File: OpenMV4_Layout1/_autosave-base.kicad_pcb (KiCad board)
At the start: 4 copper layers, 35.6 x 44.5 mm, 57 parts, among them M1 9774030243R, M2 9774030243R, Q1 BSS138, Q2 Si2301BDS, U1 STM32H743VIT6, U5 TPS731XX, U8 PAM2305AABADJ, X1 MF-CON-MICROUSB-RIGHT, X2 USD-1040310811, X3 DF12-36-DS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

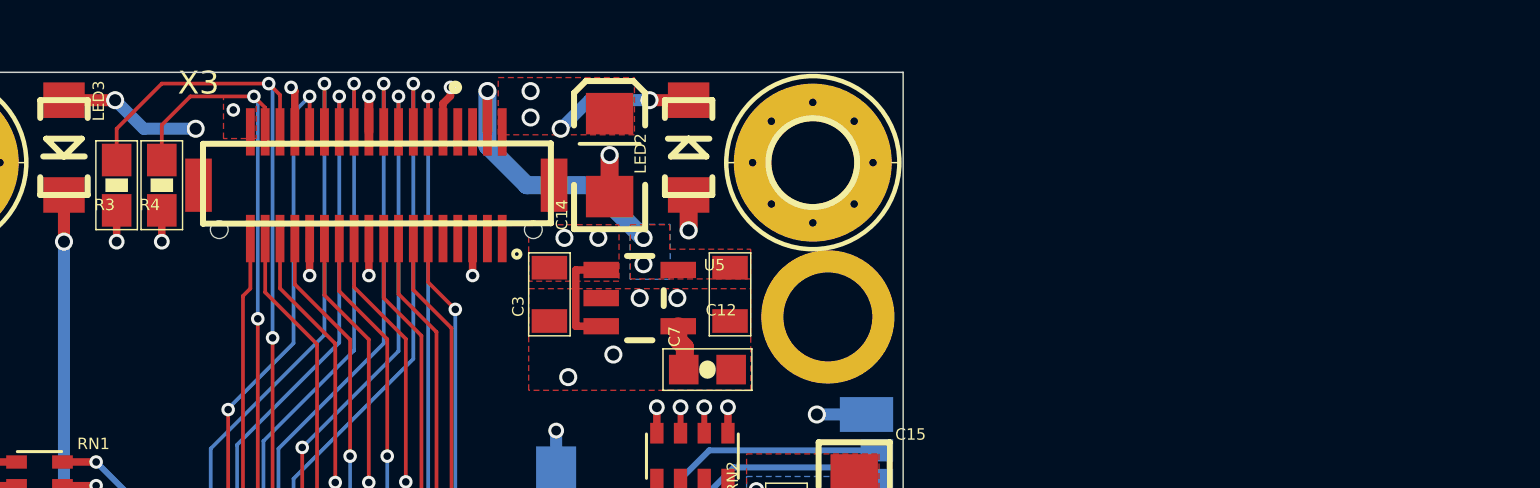
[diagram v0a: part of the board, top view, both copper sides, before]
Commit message: Swapped image sensor connector to opposite side
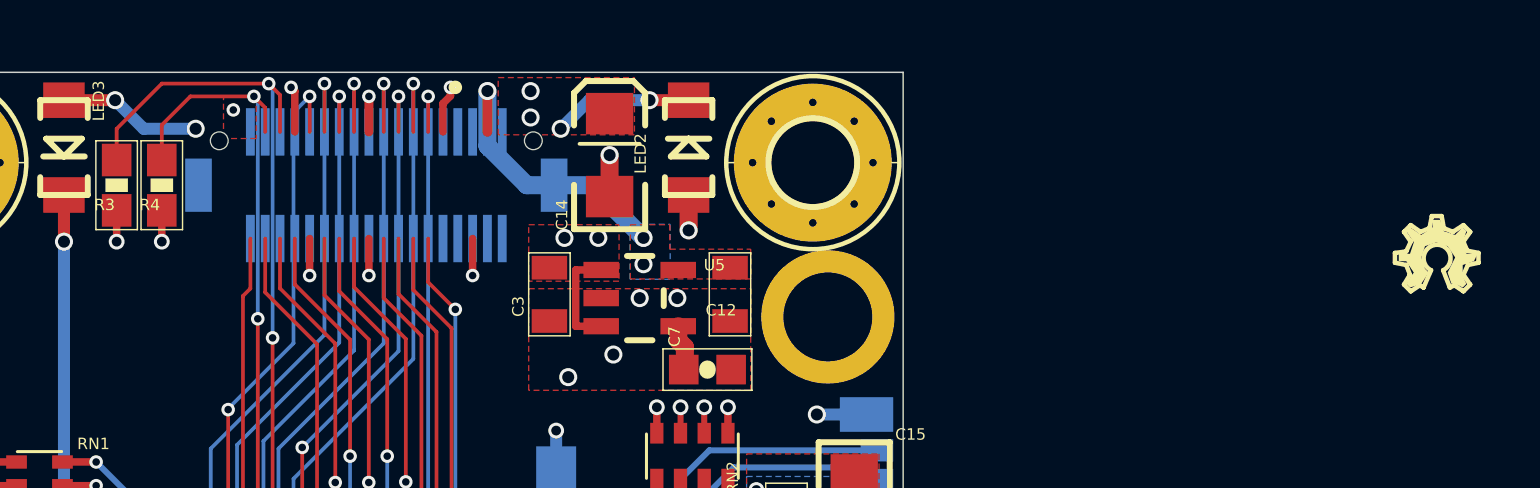
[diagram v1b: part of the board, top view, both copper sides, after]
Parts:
- added LOGO1: OSHW_LOGO_FILLX0100-NT, base:OSHW_FILLX100_NOTEXT, F.Cu at (182.9, 90.2)
- X3: moved to B.Cu

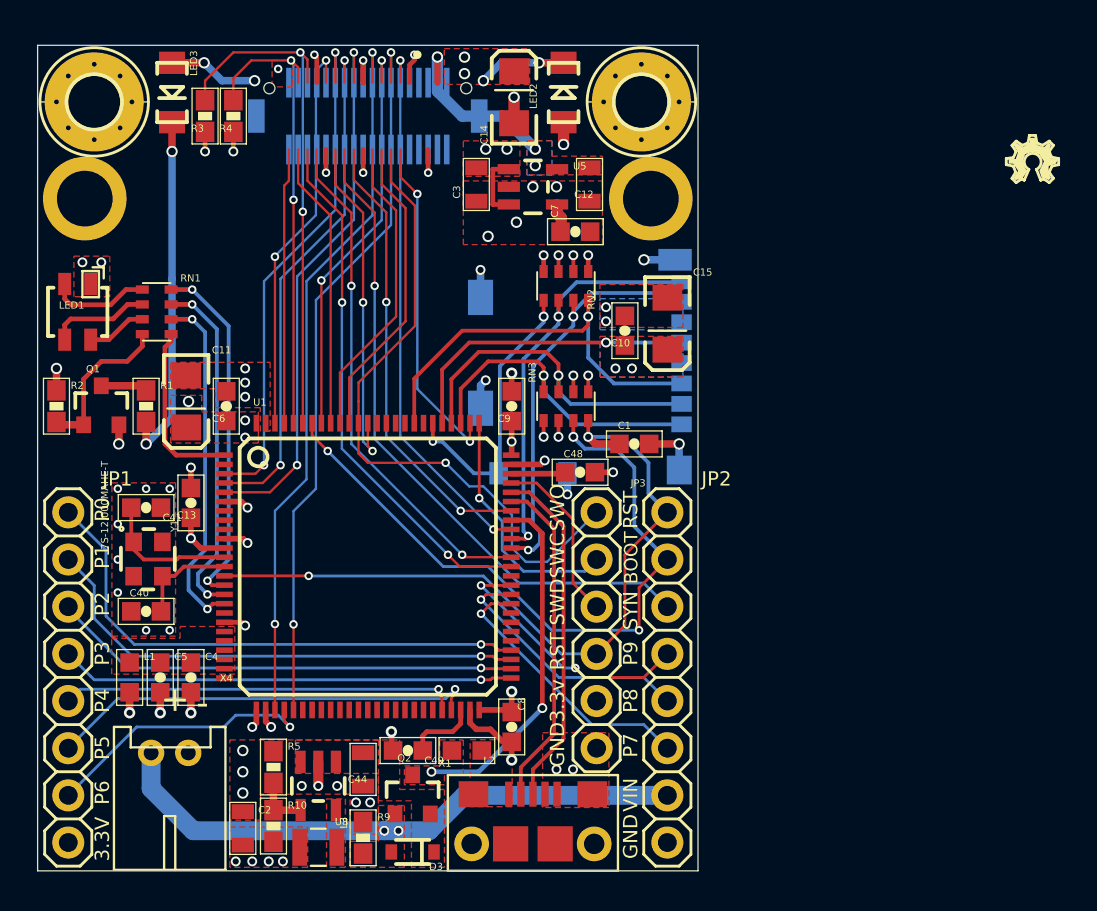
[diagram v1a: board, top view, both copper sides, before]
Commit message: Deleted connections, moved camera
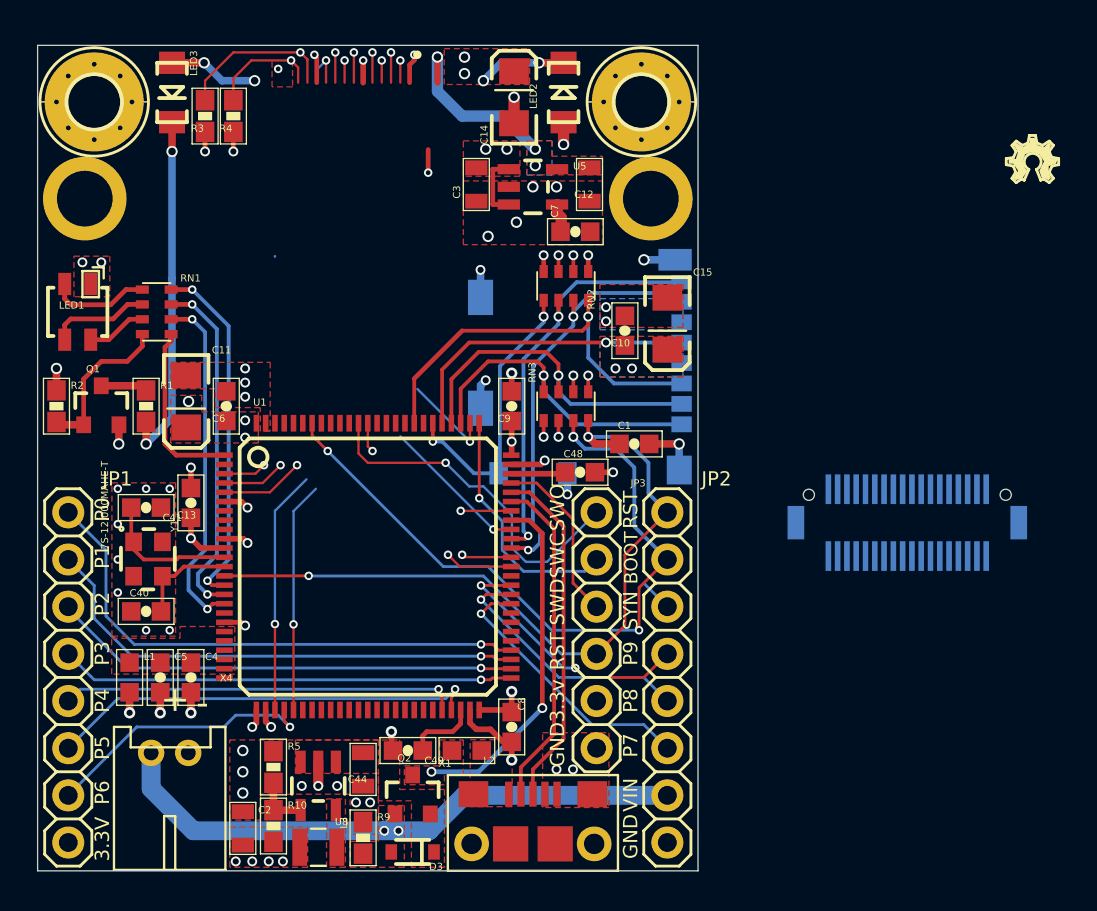
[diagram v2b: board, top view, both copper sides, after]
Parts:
- moved X3 36.4 mm to (177.6, 108.5)
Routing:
- net /DCMI_FSIN: track 35.8 -> 1.80 mm, vias 1 -> 0
- net /DCMI_PCLK: track 39.2 -> 14.0 mm
- net /DCMI_D0: track 28.6 -> 3.67 mm, vias 2 -> 1
- net /DCMI_HSYNC: track 39.2 -> 14.8 mm
- net /DCMI_D4: track 27.8 -> 3.95 mm
- net /DCMI_D7: track 29.6 -> 6.14 mm
- net /DCMI_D6: track 27.8 -> 4.62 mm
- net /DCMI_D1: track 27.8 -> 4.66 mm
- net /DCMI_RST: track 24.6 -> 2.72 mm, vias 2 -> 1
- net /DCMI_D3: track 21.9 -> 0.03 mm, vias 2 -> 0
- net /DCMI_VSYNC: track 22.1 -> 1.20 mm, vias 2 -> 1
- net /DCMI_CLK: track 29.5 -> 9.24 mm
- net /I2C1_SCL: track 28.6 -> 8.79 mm, vias 2 -> 1
- net /I2C1_SDA: track 25.6 -> 6.23 mm, vias 2 -> 1
- net /DCMI_PWDN: track 18.7 -> 1.60 mm, vias 2 -> 1
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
